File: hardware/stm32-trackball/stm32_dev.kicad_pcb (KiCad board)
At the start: 2 copper layers, 70.8 x 30 mm, 56 parts, among them J1 USB_C_Receptacle_USB2.0, J2 SWD, J3 UART, J4 SPARE, J5 Breakout, J6 Breakout, SW1 SIDE, SW2 SIDE, SW3 SW_Push, T1 Trackball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

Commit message: Rename duplicate REF** names, they mess up with DSN export and pick and place machines
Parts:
- removed the FRAME1 at (191.8, 136.4)
- removed REF** (x2): MountingHole_2.1mm, MountingHole:MountingHole_2.1mm
- added FRAME2: FRAME-LETTER1, SparkFun_Blackberry_Trackballer_Breakout_v13:CREATIVE_COMMONS, F.Cu at (191.8, 136.4)
- added mounthole1: MountingHole_2.1mm, MountingHole:MountingHole_2.1mm, F.Cu at (77.6, 89.5)
- added mounthole2: MountingHole_2.1mm, MountingHole:MountingHole_2.1mm, F.Cu at (77.6, 112.5)
- FRAME1: value FRAME-LETTER -> FRAME-LETTER2
- renumbered REF** to mounthole_trackball_1, REF** to mounthole_trackball_2, REF** to mounthole_trackball_3, REF** to mounthole_trackball_4
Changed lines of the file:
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@@
     (47 F.CrtYd user)
     (48 B.Fab user)
-    (49 F.Fab user hide)
+    (49 F.Fab user)
   )
   (setup
@@
     (pad_to_mask_clearance 0.05)
     (aux_axis_origin 0 0)
-    (visible_elements FFFFFF7F)
+    (visible_elements FFFFFFFF)
     (pcbplotparams
       (layerselection 0x010fc_ffffffff)
@@
     (tags "mounting hole 2.1mm no annular")
     (attr virtual)
-    (fp_text reference REF** (at 0 -3.2) (layer F.SilkS) hide
+    (fp_text reference mounthole1 (at 0 -3.2) (layer F.SilkS) hide
       (effects (font (size 1 1) (thickness 0.15)))
     )
@@
     (tags "mounting hole 2.1mm no annular")
     (attr virtual)
-    (fp_text reference REF** (at 0 -3.2) (layer F.SilkS) hide
+    (fp_text reference mounthole2 (at 0 -3.2) (layer F.SilkS) hide
       (effects (font (size 1 1) (thickness 0.15)))
     )
@@
     (tags "mounting hole 2.1mm no annular")
     (attr virtual)
-    (fp_text reference REF** (at 0 -3.2) (layer F.SilkS) hide
+    (fp_text reference mounthole_trackball_2 (at 0 -3.2) (layer F.SilkS) hide
       (effects (font (size 1 1) (thickness 0.15)))
     )
@@
     (tags "mounting hole 2.1mm no annular")
     (attr virtual)
-    (fp_text reference REF** (at 0 -3.2) (layer F.SilkS) hide
+    (fp_text reference mounthole_trackball_1 (at 0 -3.2) (layer F.SilkS) hide
       (effects (font (size 1 1) (thickness 0.15)))
     )
@@
     (tags "mounting hole 2.1mm no annular")
     (attr virtual)
-    (fp_text reference REF** (at 0 -3.2) (layer F.SilkS) hide
+    (fp_text reference mounthole_trackball_4 (at 0 -3.2) (layer F.SilkS) hide
       (effects (font (size 1 1) (thickness 0.15)))
     )
@@
     (tags "mounting hole 2.1mm no annular")
     (attr virtual)
-    (fp_text reference REF** (at 0 -3.2) (layer F.SilkS) hide
+    (fp_text reference mounthole_trackball_3 (at 0 -3.2) (layer F.SilkS) hide
       (effects (font (size 1 1) (thickness 0.15)))
     )
@@
   (module SparkFun_Blackberry_Trackballer_Breakout_v13:CREATIVE_COMMONS (layer Top)
     (at 191.678979 136.3186)
-    (fp_text reference FRAME1 (at 0 0) (layer F.SilkS) hide
+    (fp_text reference FRAME1 (at 0.141021 -2.1586) (layer F.SilkS) hide
       (effects (font (size 1.27 1.27) (thickness 0.15)))
     )
-    (fp_text value FRAME-LETTER (at 0 0) (layer F.SilkS) hide
+    (fp_text value FRAME-LETTER2 (at 0.131021 2.5914) (layer F.SilkS) hide
       (effects (font (size 1.27 1.27) (thickness 0.15)))
     )
@@
   (module SparkFun_Blackberry_Trackballer_Breakout_v13:CREATIVE_COMMONS (layer Top)
     (at 191.828979 136.3686)
-    (fp_text reference FRAME1 (at 0 0) (layer F.SilkS) hide
+    (fp_text reference FRAME2 (at 7.251021 -2.2886) (layer F.SilkS) hide
       (effects (font (size 1.27 1.27) (thickness 0.15)))
     )
-    (fp_text value FRAME-LETTER (at 0 0) (layer F.SilkS) hide
+    (fp_text value FRAME-LETTER1 (at 0 0) (layer F.SilkS) hide
       (effects (font (size 1.27 1.27) (thickness 0.15)))
     )

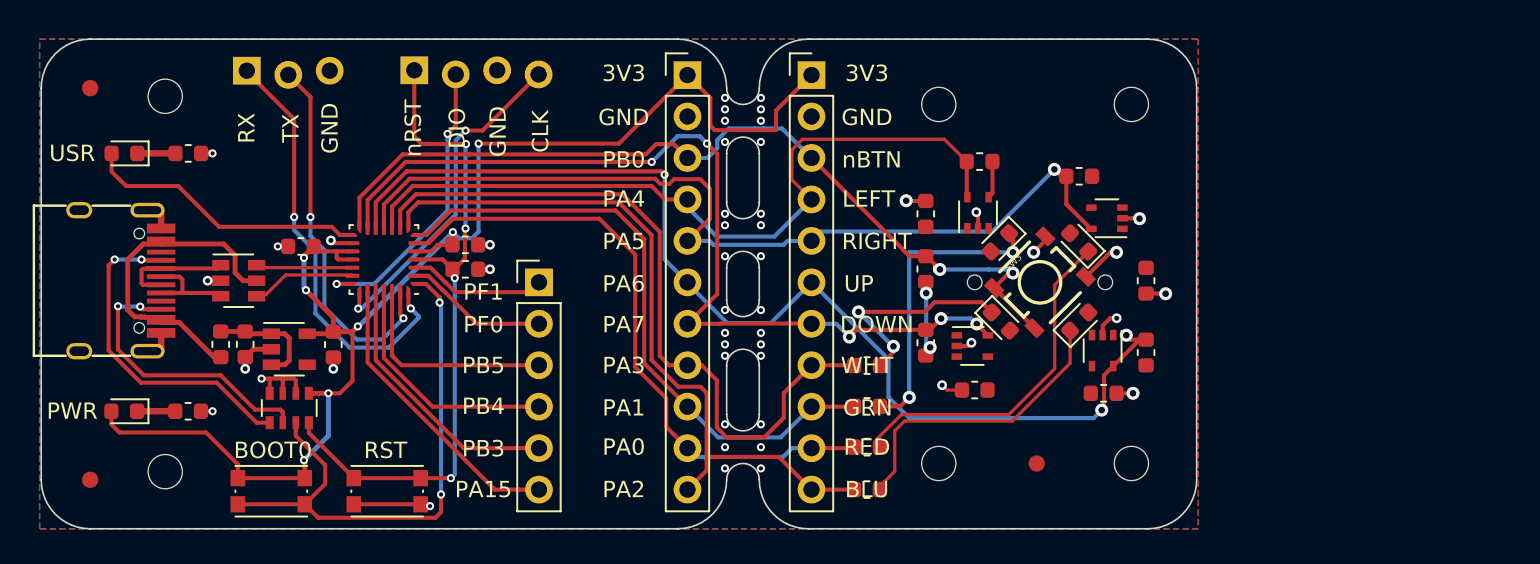
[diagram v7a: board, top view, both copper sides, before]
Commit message: add mounting holes to schematic, improve decoupling cap placement
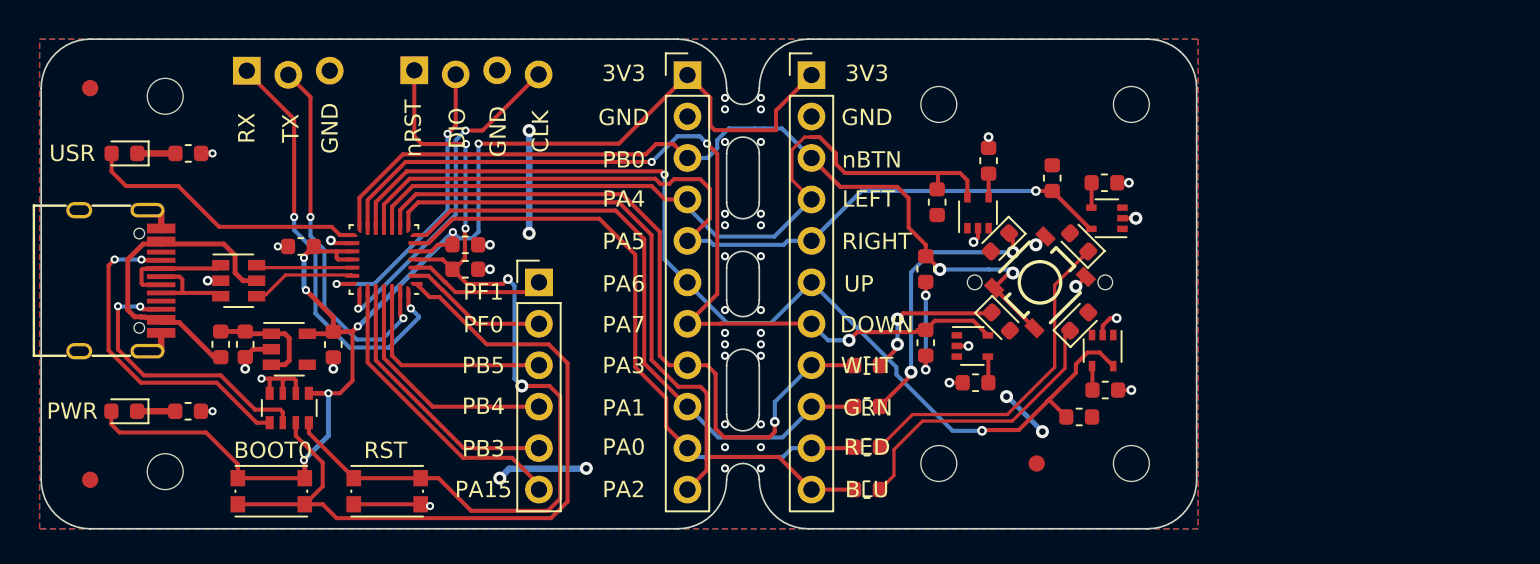
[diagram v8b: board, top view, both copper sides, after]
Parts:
- removed FRAME1: FRAME-LETTER2, SparkFun_Blackberry_Trackballer_Breakout_v13:CREATIVE_COMMONS
- removed FRAME2: FRAME-LETTER1, SparkFun_Blackberry_Trackballer_Breakout_v13:CREATIVE_COMMONS
- removed mounthole1, mounthole2, mounthole_trackball_1, mounthole_trackball_2, mounthole_trackball_3, mounthole_trackball_4: MountingHole_2.1mm, MountingHole:MountingHole_2.1mm
- added H4: M2, MountingHole:MountingHole_2.2mm_M2, F.Cu at (125.0, 90.0)
- added H5: M2, MountingHole:MountingHole_2.2mm_M2, F.Cu at (77.6, 112.5)
- added H6: M2, MountingHole:MountingHole_2.2mm_M2, F.Cu at (77.6, 89.5)
- added H7: M2, MountingHole:MountingHole_2.2mm_M2, F.Cu at (125.0, 112.0)
- added H8: M2, MountingHole:MountingHole_2.2mm_M2, F.Cu at (136.8, 90.0)
- added H9: M2, MountingHole:MountingHole_2.2mm_M2, F.Cu at (136.8, 112.0)
- moved C10 6.52 mm to (135.2, 94.8), turned to 0 degrees
- moved R4 5.69 mm to (133.6, 109.2), turned to 180 degrees
- moved C9 5.04 mm to (128.1, 93.5)
- moved R3 3.60 mm to (124.9, 96.0), turned to 90 degrees
- moved R5 1.65 mm to (131.9, 94.5), turned to 270 degrees
- moved C8 0.45 mm to (127.2, 107.0)
- moved C7 0.22 mm to (135.2, 107.5)
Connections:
- J1 pad A8: Net-(J1-PadA8) -> (no net)
- J1 pad B8: Net-(J1-PadB8) -> (no net)
- U1 pad 4: Net-(U1-Pad4) -> (no net)
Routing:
- net +3V3: track 92.1 -> 111.8 mm, vias 9 -> 15
- net /nRST: track 41.5 -> 56.0 mm
- net /BOOT0: track 34.2 -> 46.9 mm, vias 2 -> 0
- net GND: track 35.8 -> 31.5 mm, vias 33 -> 31
- net Net-(D6-Pad1): track 13.3 -> 9.37 mm
- net /TB_RIGHT: track 66.8 -> 64.0 mm, vias 3 -> 2
- net /TB_UP: track 55.6 -> 53.5 mm
- net Net-(D5-Pad1): track 18.5 -> 17.0 mm
- net /nTB_BUTTON: track 53.9 -> 55.4 mm
- net /TB_LEFT: track 47.3 -> 48.4 mm
- net Net-(D3-Pad1): track 18.8 -> 17.8 mm
- net /nLED_WHT: track 44.2 -> 44.6 mm, vias 0 -> 1
- net /TB_DOWN: vias 5 -> 3
